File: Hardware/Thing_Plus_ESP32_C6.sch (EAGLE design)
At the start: 55 parts, among them J1 THING_PLUS_LOGICAL, J4 QWIIC_RIGHT_ANGLE, J5 MICRO-SDFRICTION, Q1 20V/4.2A/52mΩ/1.4W, U1 ESP32-C6-WROOM-1-NARROW, U2 RT9080-33GJ5, U3 MCP73831, U4 MAX17048

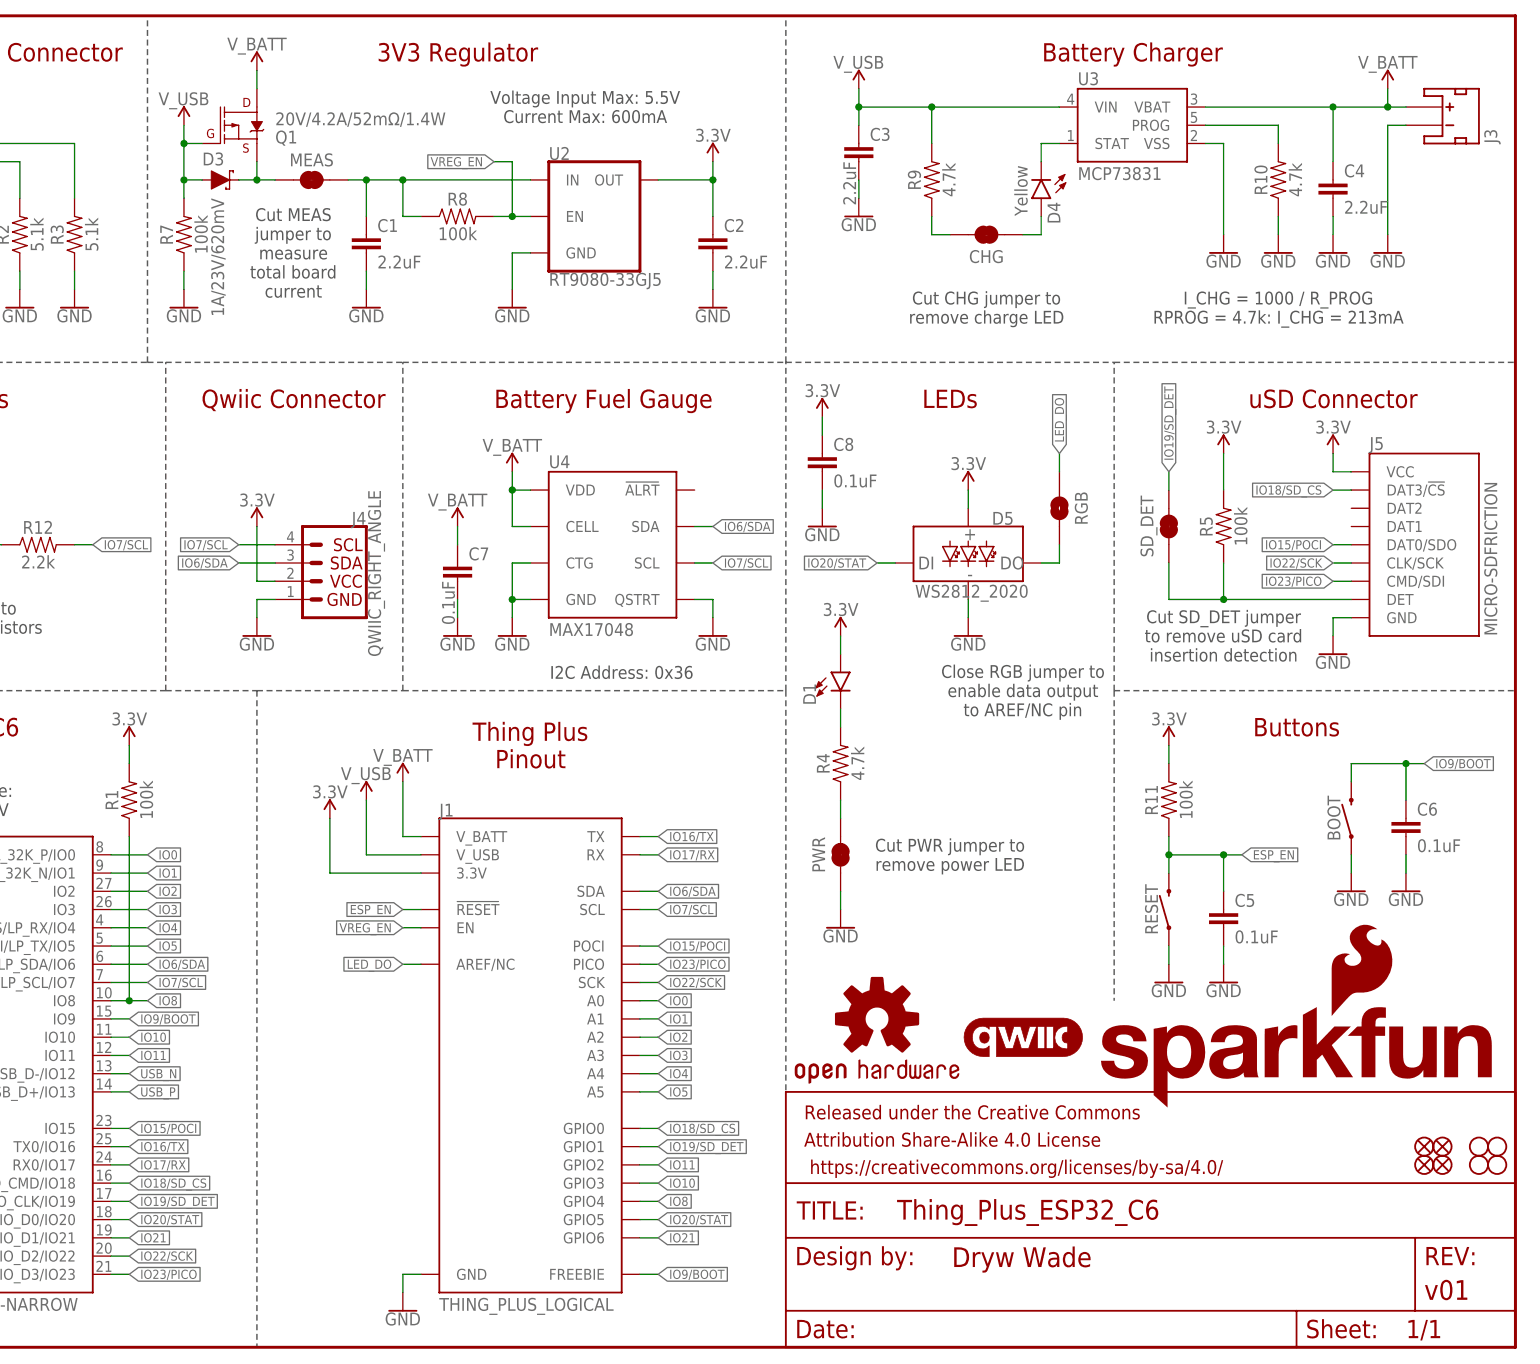
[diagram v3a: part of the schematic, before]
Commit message: Add power control to uSD card
Also add 10uF cap for uSD card
And add boot button text
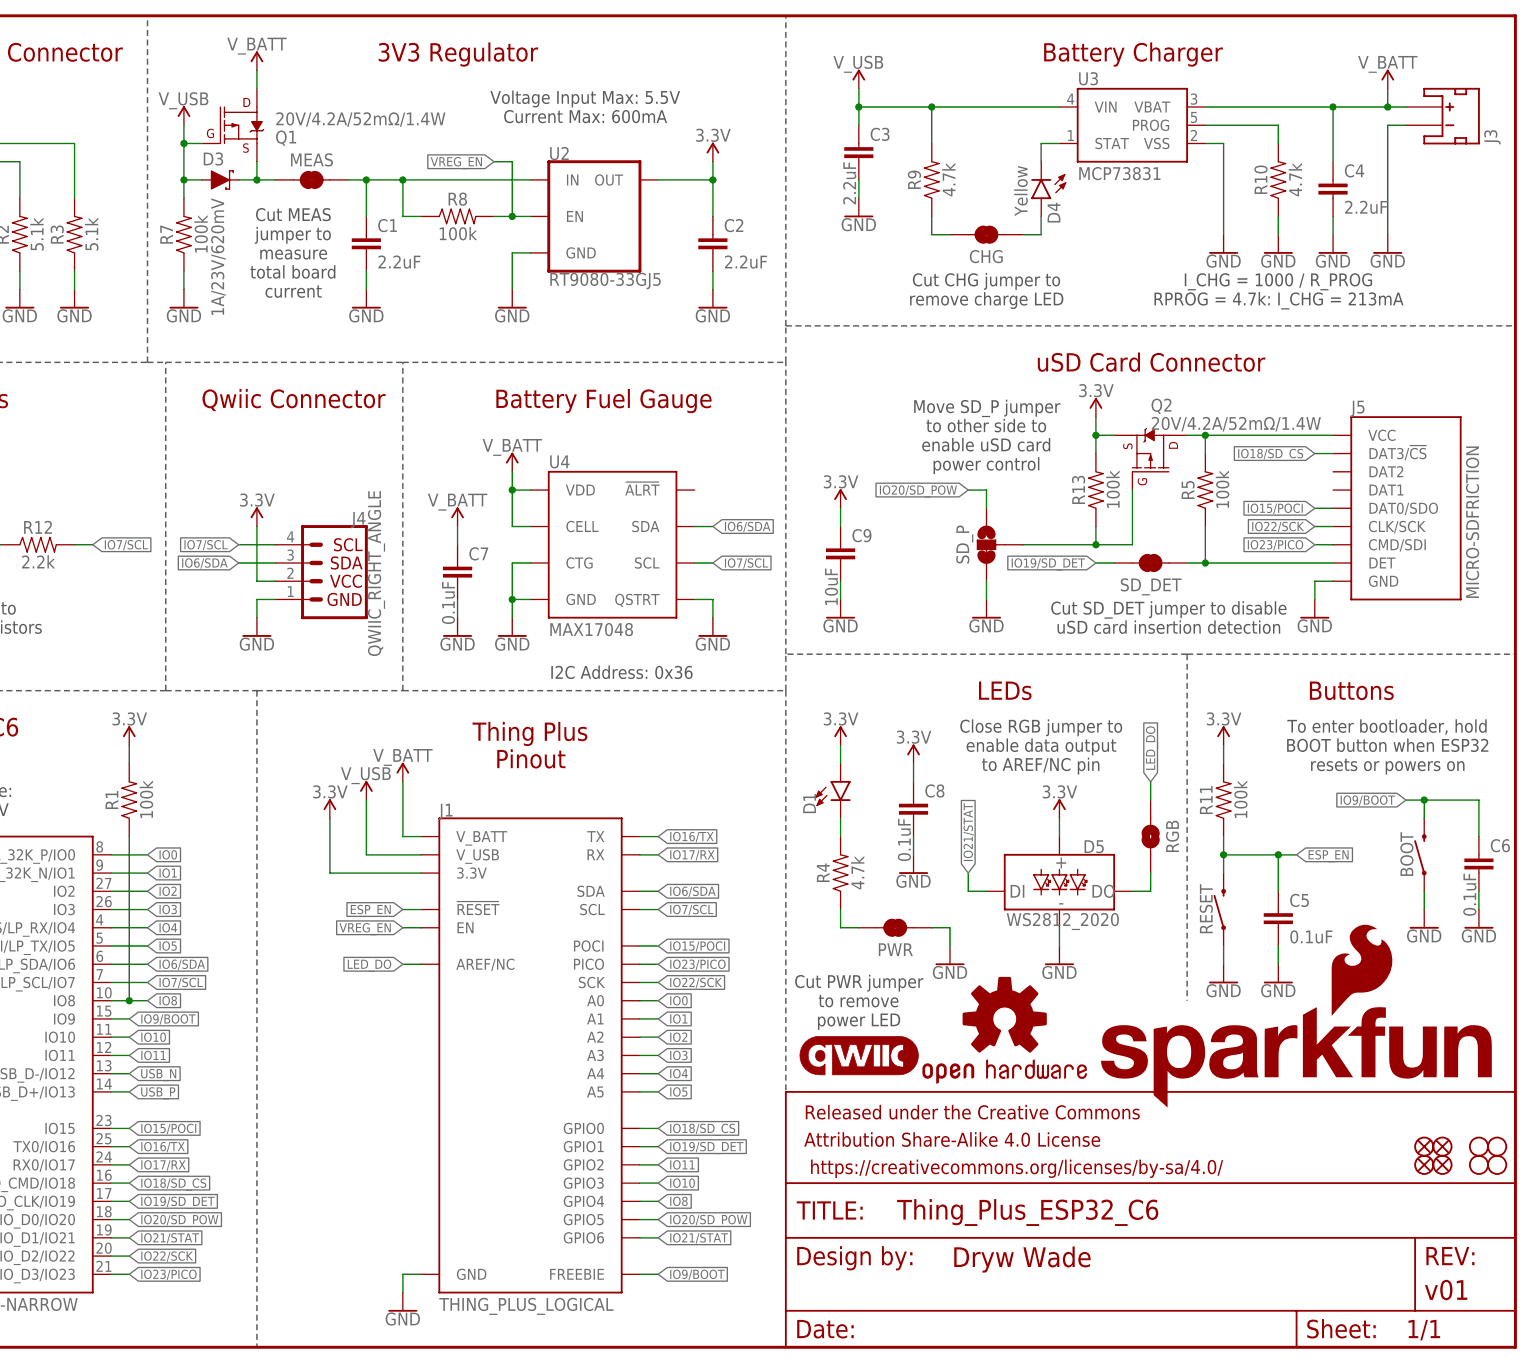
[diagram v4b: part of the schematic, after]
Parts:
- added C9: 10uF, SparkFun-Capacitors:10UF-0603-6.3V-20%
- added Q2: 20V/4.2A/52mΩ/1.4W, SparkFun-DiscreteSemi:MOSFET_PCH-DMG2305UX-7
- added R13: 100k, SparkFun-Resistors:100KOHM-0603-1/10W-1%
- added SD_P: JUMPER-SMT_3_1-NC_TRACE_SILK, SparkFun-Jumpers:JUMPER-SMT_3_1-NC_TRACE_SILK
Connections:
- removed net IO20/STAT: D5.DI, J1.GPIO5, U1.SDIO_D0/IO20
- removed net IO21: J1.GPIO6, U1.SDIO_D1/IO21
- new net IO20/SD_POW: J1.GPIO5, SD_P.1, U1.SDIO_D0/IO20
- new net IO21/STAT: D5.DI, J1.GPIO6, U1.SDIO_D1/IO21
- new net N$15: J5.VCC, Q2.D, R5.2
- new net N$16: Q2.G, R13.1, SD_P.2
- net 3.3V: now also C9.1, Q2.S, R13.2; no longer J5.VCC, R5.2
- net GND: now also C9.2, SD_P.3
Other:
- note added: "Cut SD_DET jumper to disable uSD card insertion detection"
- note added: "Move SD_P jumper to other side to enable uSD card power control"
- note added: "To enter bootloader, hold BOOT button when ESP32 resets or powers on"
- note added: "uSD Card Connector"
- note removed: "Cut SD_DET jumper to remove uSD card insertion detection"
- note removed: "uSD Connector"
- moved on the sheet: BOOT, C5, C6, C8, D1, D5, J5, PWR, R11, R4, R5, RESET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

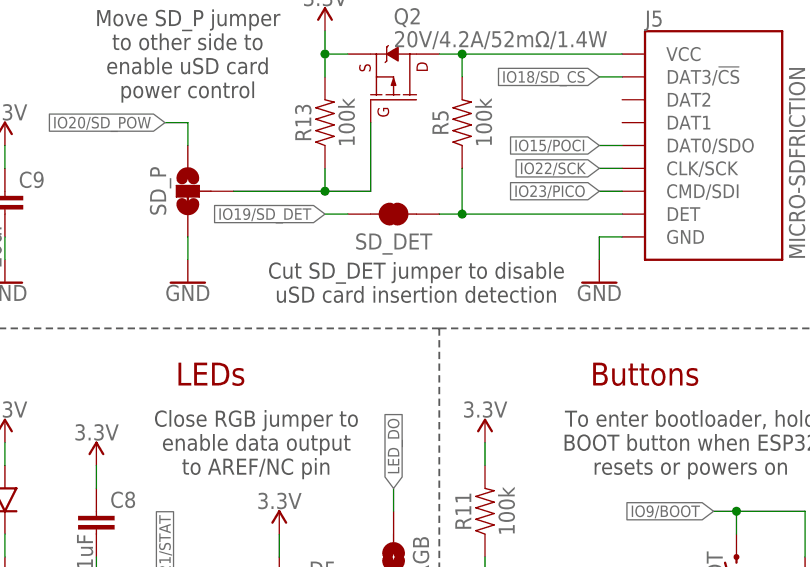
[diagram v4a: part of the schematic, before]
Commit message: Checklist updates
Add version number to copper
Fix dimension lines to be exactly on grid
Add PROD_ID to ESP32-C6 narrow device
Add layer numbers to copper
Add silk labels to SD_P jumper
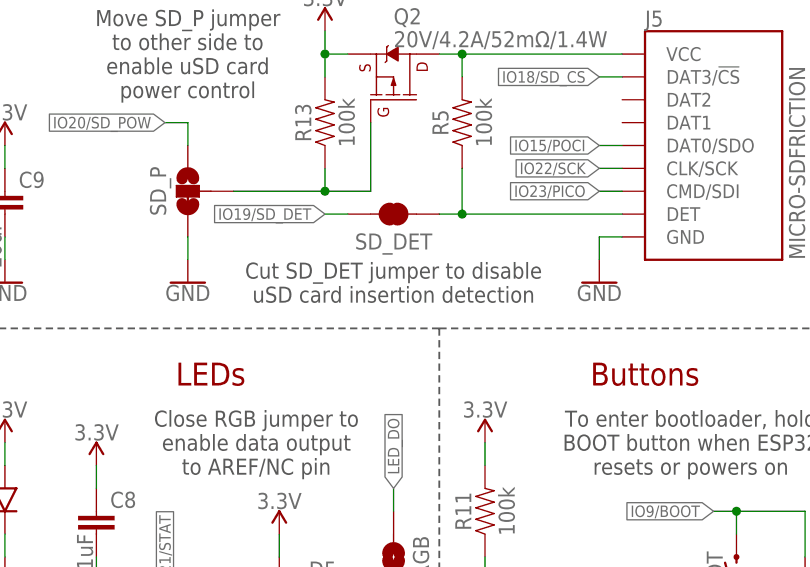
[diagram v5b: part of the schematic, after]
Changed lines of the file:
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@@
 <text x="119.38" y="172.72" size="1.778" layer="97" font="vector" align="center">Voltage Input Max: 5.5V
 Current Max: 600mA</text>
-<text x="200.66" y="101.6" size="1.778" layer="97" font="vector" align="center">Cut SD_DET jumper to disable
+<text x="198.12" y="101.6" size="1.778" layer="97" font="vector" align="center">Cut SD_DET jumper to disable
 uSD card insertion detection</text>
 <text x="182.88" y="83.82" size="1.778" layer="97" font="vector" align="center">Close RGB jumper to

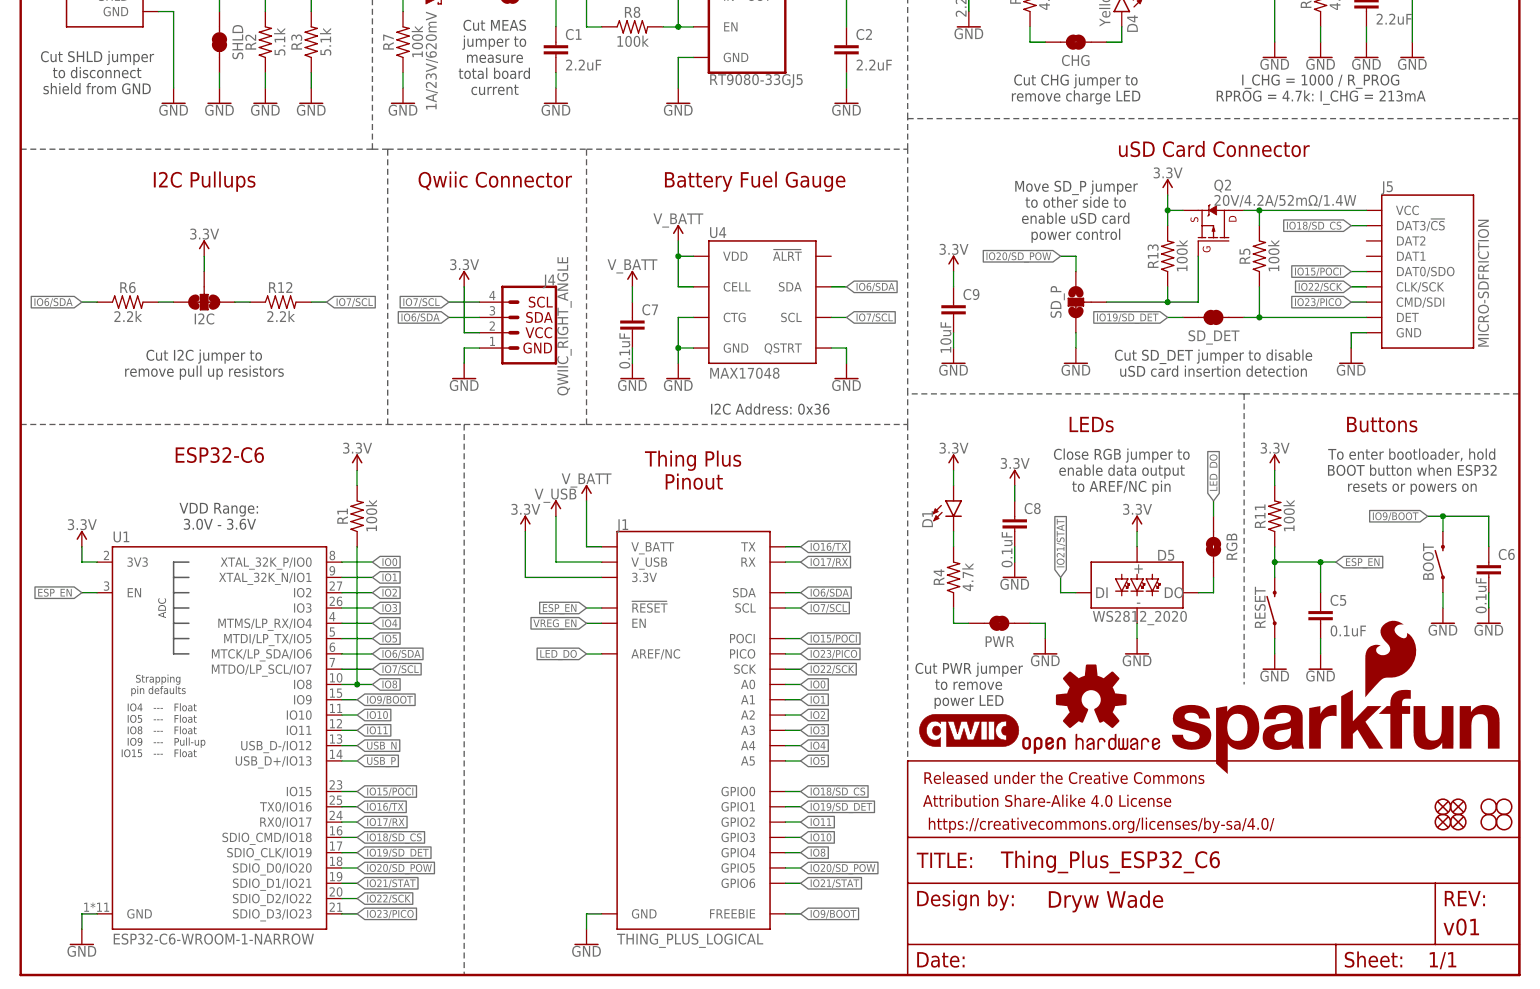
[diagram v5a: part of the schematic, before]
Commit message: v10 updates
Change pinout of GPIO 15-23 (SDIO pins have funky behavior when not configured)
Connect fuel gauge alert pin
Move SD power control to own circuit that creates VOUT net
Change STAT LED to get powered from VOUT
Change RGB jumper to NC
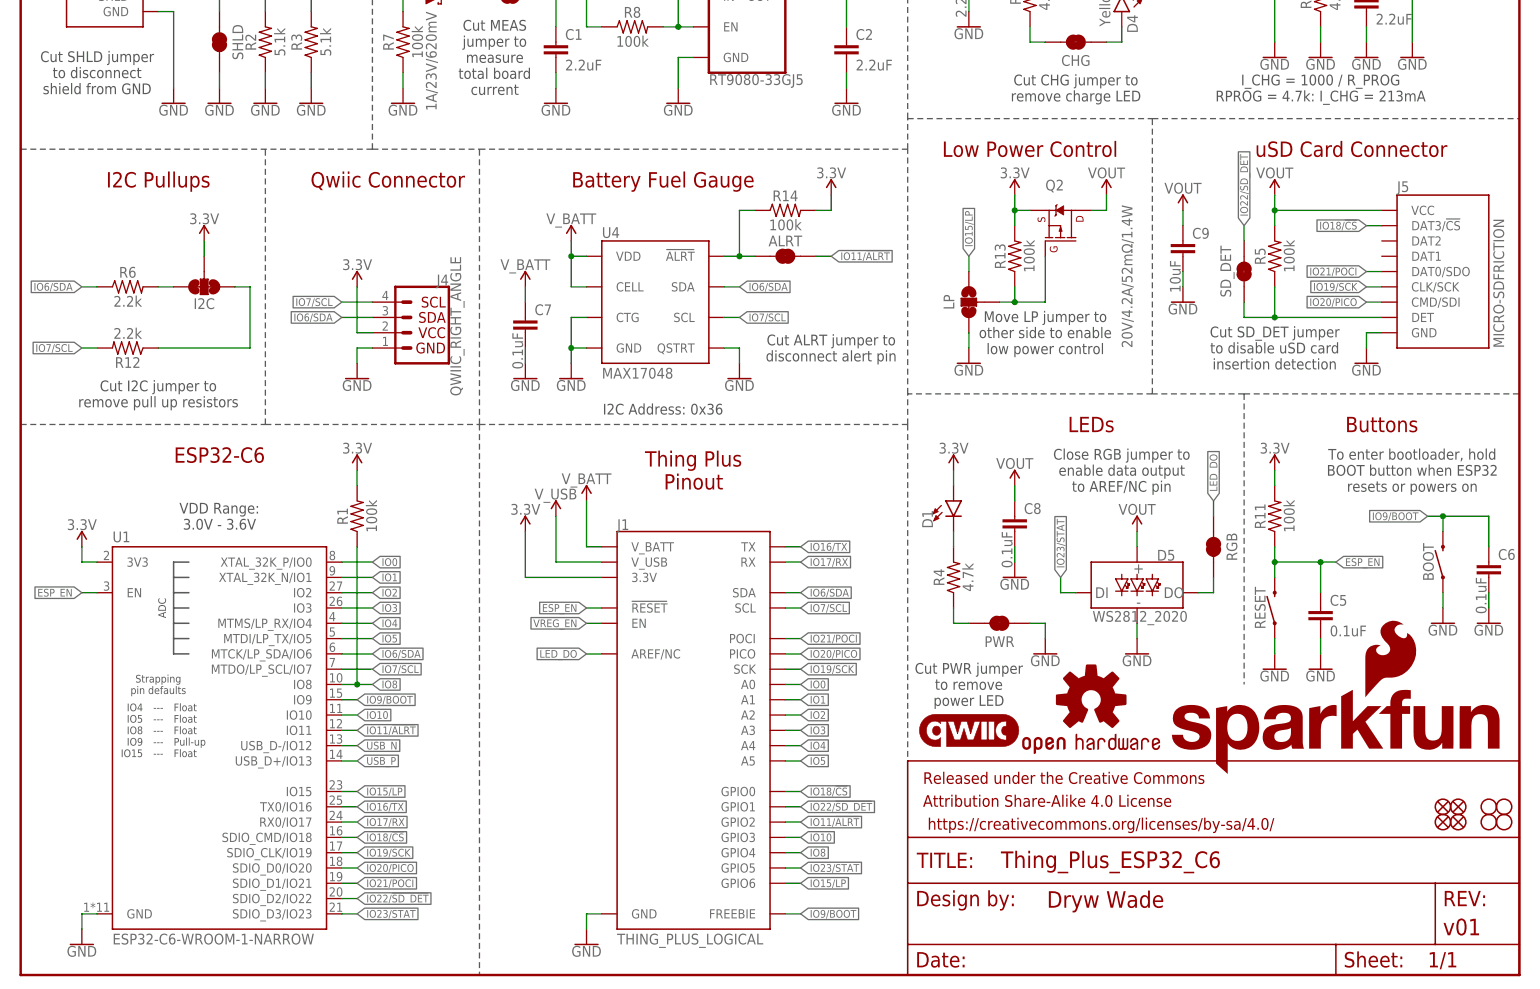
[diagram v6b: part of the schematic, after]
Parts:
- removed SD_P: JUMPER-SMT_3_1-NC_TRACE_SILK, SparkFun-Jumpers:JUMPER-SMT_3_1-NC_TRACE_SILK
- added ALRT: JUMPER-SMT_2_NC_TRACE_SILK, SparkFun-Jumpers:JUMPER-SMT_2_NC_TRACE_SILK
- added LP: JUMPER-SMT_3_1-NC_TRACE_SILK, SparkFun-Jumpers:JUMPER-SMT_3_1-NC_TRACE_SILK
- added R14: 100k, SparkFun-Resistors:100KOHM-0603-1/10W-1%
- RGB: value JUMPER-SMT_2_NO_SILK -> JUMPER-SMT_2_NC_TRACE_SILK; device SparkFun-Jumpers:JUMPER-SMT_2_NO_SILK -> SparkFun-Jumpers:JUMPER-SMT_2_NC_TRACE_SILK
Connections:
- net IO18/SD_CS renamed IO18/!CS!
- removed net IO11: J1.GPIO2, U1.IO11
- removed net IO15/POCI: J1.POCI, J5.DAT0/SDO, U1.IO15
- removed net IO19/SD_DET: J1.GPIO1, SD_DET.2, U1.SDIO_CLK/IO19
- removed net IO20/SD_POW: J1.GPIO5, SD_P.1, U1.SDIO_D0/IO20
- removed net IO21/STAT: D5.DI, J1.GPIO6, U1.SDIO_D1/IO21
- removed net IO22/SCK: J1.SCK, J5.CLK/SCK, U1.SDIO_D2/IO22
- removed net IO23/PICO: J1.PICO, J5.CMD/SDI, U1.SDIO_D3/IO23
- removed net N$15: J5.VCC, Q2.D, R5.2
- new net IO11/!ALRT!: ALRT.2, J1.GPIO2, U1.IO11
- new net IO15/LP: J1.GPIO6, LP.1, U1.IO15
- new net IO19/SCK: J1.SCK, J5.CLK/SCK, U1.SDIO_CLK/IO19
- new net IO20/PICO: J1.PICO, J5.CMD/SDI, U1.SDIO_D0/IO20
- new net IO21/POCI: J1.POCI, J5.DAT0/SDO, U1.SDIO_D1/IO21
- new net IO22/!SD_DET!: J1.GPIO1, SD_DET.2, U1.SDIO_D2/IO22
- new net IO23/STAT: D5.DI, J1.GPIO5, U1.SDIO_D3/IO23
- new net N$17: ALRT.1, R14.1, U4.!ALRT
- new net VOUT: C8.1, C9.1, D5.VCC, J5.VCC, Q2.D, R5.2
- net 3.3V: now also R14.2; no longer C8.1, C9.1, D5.VCC
- net GND: now also LP.3; no longer SD_P.3
- net N$16: now also LP.2; no longer SD_P.2
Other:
- note added: "Cut ALRT jumper to disconnect alert pin"
- note added: "Low Power Control"
- note added: "Move LP jumper to other side to enable low power control"
- note removed: "Move SD_P jumper to other side to enable uSD card power control"
- moved on the sheet: C7, C9, I2C, J4, J5, Q2, R12, R13, R5, R6, SD_DET, U4

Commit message: Bump version number to v10
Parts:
- FRAME1: REV v01 -> v10
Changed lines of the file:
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@@
 <part name="FRAME1" library="SparkFun-Aesthetics" deviceset="FRAME-LETTER" device="">
 <attribute name="DESIGNER" value="Dryw Wade"/>
-<attribute name="REV" value="v01"/>
+<attribute name="REV" value="v10"/>
 </part>
 <part name="U1" library="ESP32-C6-WROOM-1" deviceset="ESP32-C6-WROOM-1" device="-NARROW" value="ESP32-C6-WROOM-1-NARROW"/>

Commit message: Design review updates
Change schematic frame to ledger
Fix acid trap
Approve DRC errors on jumpers
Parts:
- FRAME1: value FRAME-LETTER -> FRAME-LEDGER; device SparkFun-Aesthetics:FRAME-LETTER -> SparkFun-Aesthetics:FRAME-LEDGER
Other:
- note added: "Cut MEAS jumper to measure total board current consumption"
- note added: "Cut RGB jumper to disconect data output to AREF/NC pin"
- note added: "Move LP jumper to IO15 side to enable low power control"
- note added: "Power LED"
- note added: "Status LED"
- note removed: "Close RGB jumper to enable data output to AREF/NC pin"
- note removed: "Cut MEAS jumper to measure total board current"
- note removed: "LEDs"
- note removed: "Move LP jumper to other side to enable low power control"
- moved on the sheet: ALRT, BOOT, C1, C2, C3, C4, C5, C6, C7, C8, C9, CHG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
